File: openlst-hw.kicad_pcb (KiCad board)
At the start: 4 copper layers, 50 x 28.8 mm, 65 parts, among them J3 Conn_02x10_Odd_Even, J6 ANT, U2 CC1110, U4 ASFL1-27.000MHZ, U5 MIC803, U6 PE4250, U7 RFFM6406, U8 SF2446E

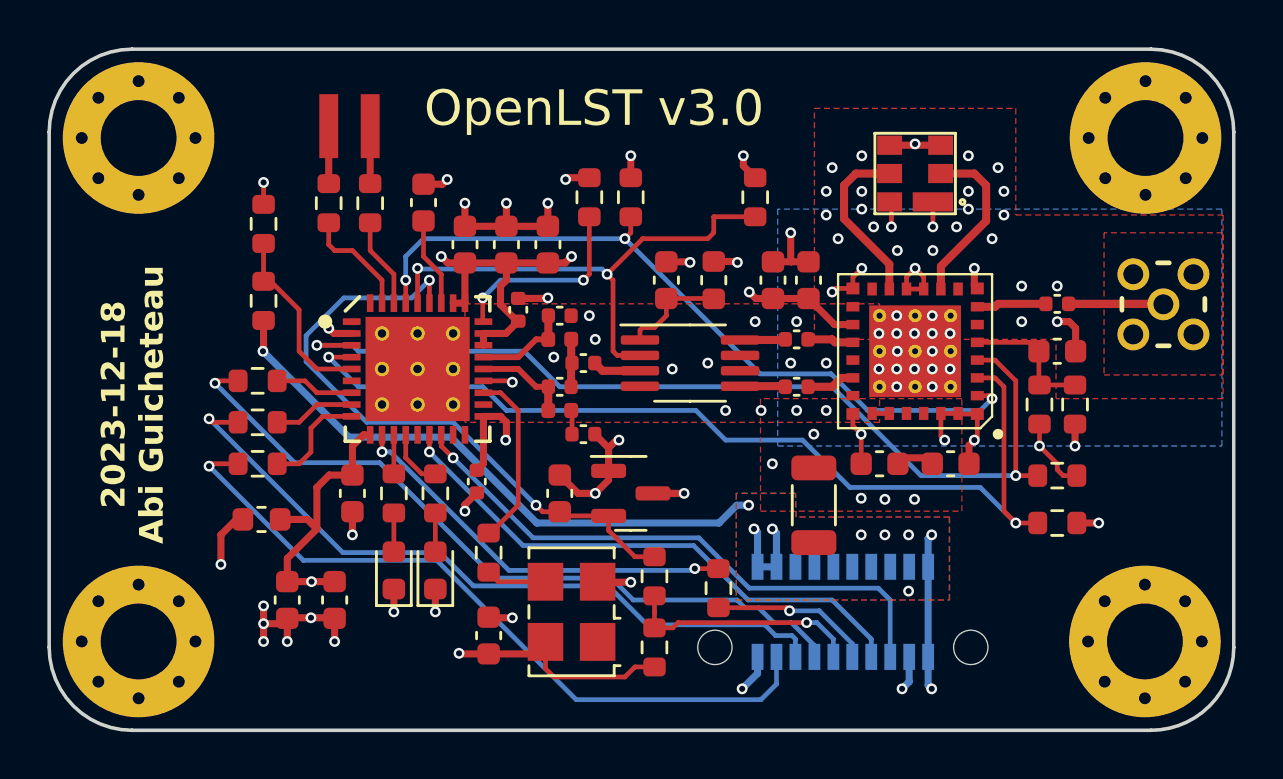
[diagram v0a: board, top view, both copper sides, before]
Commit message: added thermal reliefs and thermistors
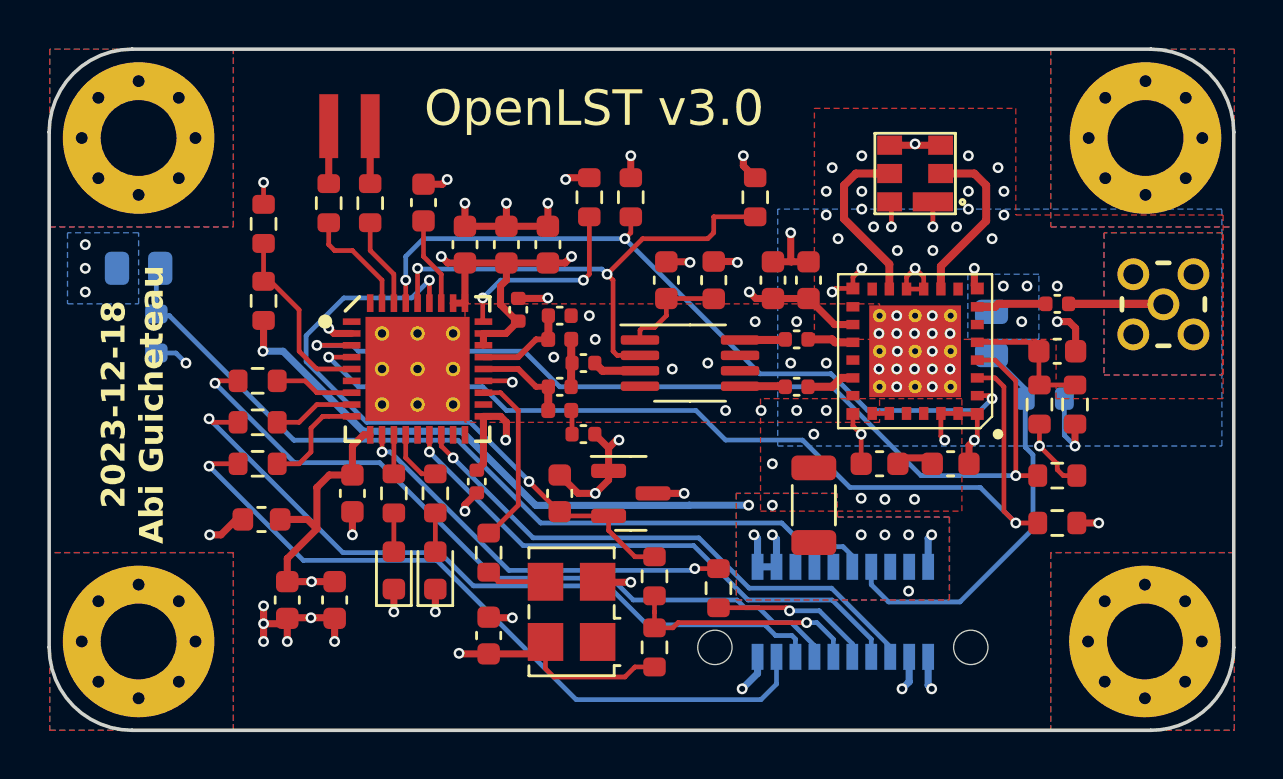
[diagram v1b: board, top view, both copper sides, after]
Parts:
- added R10: 10k, Resistor_SMD:R_0603_1608Metric, B.Cu at (141.8, 98.8)
- added R9: 10k, Resistor_SMD:R_0603_1608Metric, B.Cu at (179.2, 101.5)
- added TH1: Thermistor_NTC, Resistor_SMD:R_0805_2012Metric, B.Cu at (177.0, 98.8)
- added TH2: Thermistor_NTC, Resistor_SMD:R_0805_2012Metric, B.Cu at (141.0, 96.0)
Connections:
- J3 pad 7: unconnected-(J3-Pin_7-Pad7) -> TEMP_OUT_0
- J3 pad 9: unconnected-(J3-Pin_9-Pad9) -> TEMP_OUT_1
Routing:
- net TEMP_OUT_1: track 0.00 -> 35.9 mm
- net TEMP_OUT_0: track 0.00 -> 17.2 mm
- net GND: track 67.8 -> 63.5 mm, vias 91 -> 95
- net +3V3: track 19.5 -> 22.3 mm, vias 8 -> 9
- net /PROG_DC: track 24.5 -> 23.4 mm
- net VAA: track 25.1 -> 24.5 mm, vias 6 -> 7
